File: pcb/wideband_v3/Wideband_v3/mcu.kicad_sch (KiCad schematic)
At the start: 42 parts, among them J1 Conn_01x10, J2 USB_C_Receptacle_USB2.0, J3 Tag connect, SW1 Key0, SW3 Key1, U1 RP2040, U2 W25Q128JVS, U8 AMS1117-3.3, Y1 12MHz

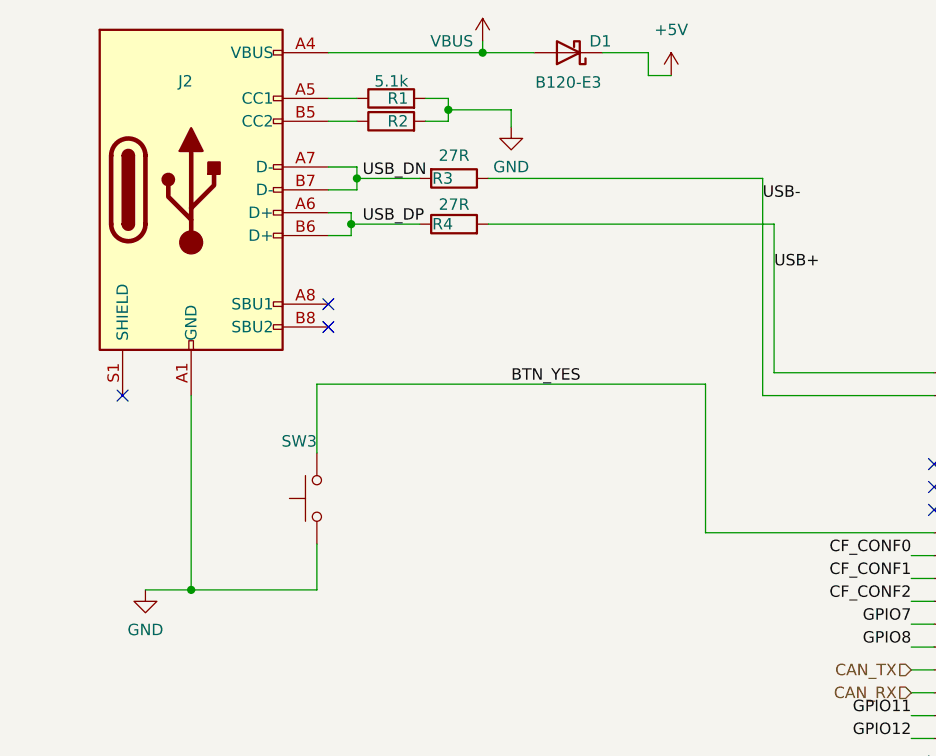
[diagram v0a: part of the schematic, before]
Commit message: rev3, reduce extended component count
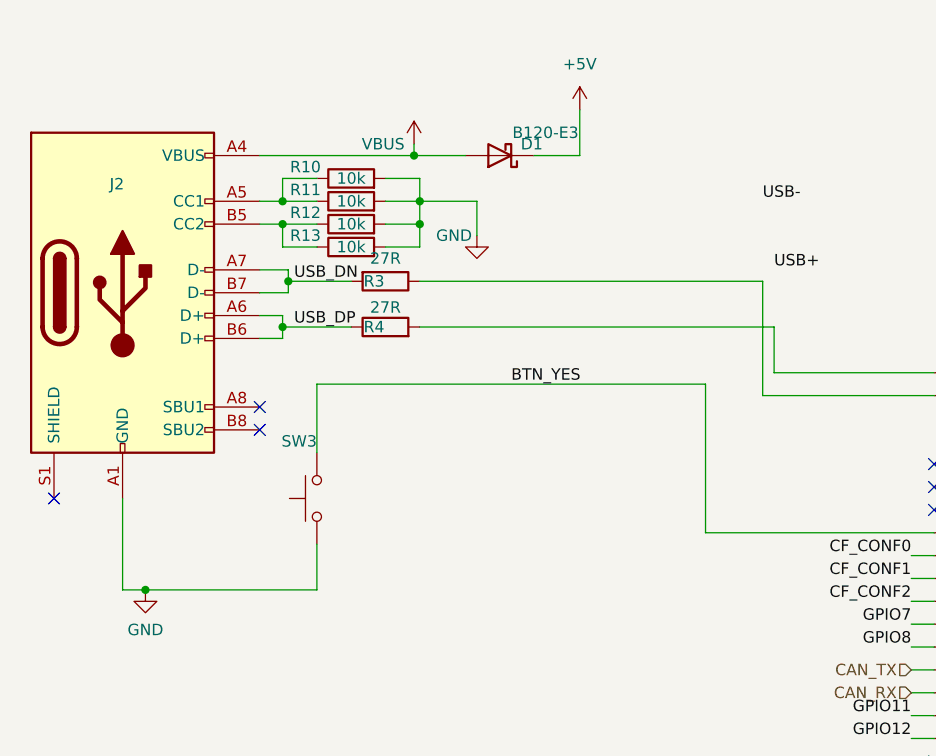
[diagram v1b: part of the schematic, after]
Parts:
- removed R1, R2: 5.1k, Resistor_SMD:R_0603_1608Metric, symbol Device:R
- added R10, R11, R12, R13: 10k, Resistor_SMD:R_0603_1608Metric, symbol Device:R
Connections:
- net GND: now also R10.2, R11.2, R12.2, R13.2
- net USB+: no longer R4.2, U1.47 (USB_DP)
- net USB-: no longer R3.1, U1.46 (USB_DM)
- net at J2.A5 (CC1): now also R10.1, R11.1
- net at J2.B5 (CC2): now also R12.1, R13.1
- new net: R3.1, U1.46 (USB_DM)
- new net: R4.2, U1.47 (USB_DP)
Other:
- moved on the sheet: D1, J2, R3, R4

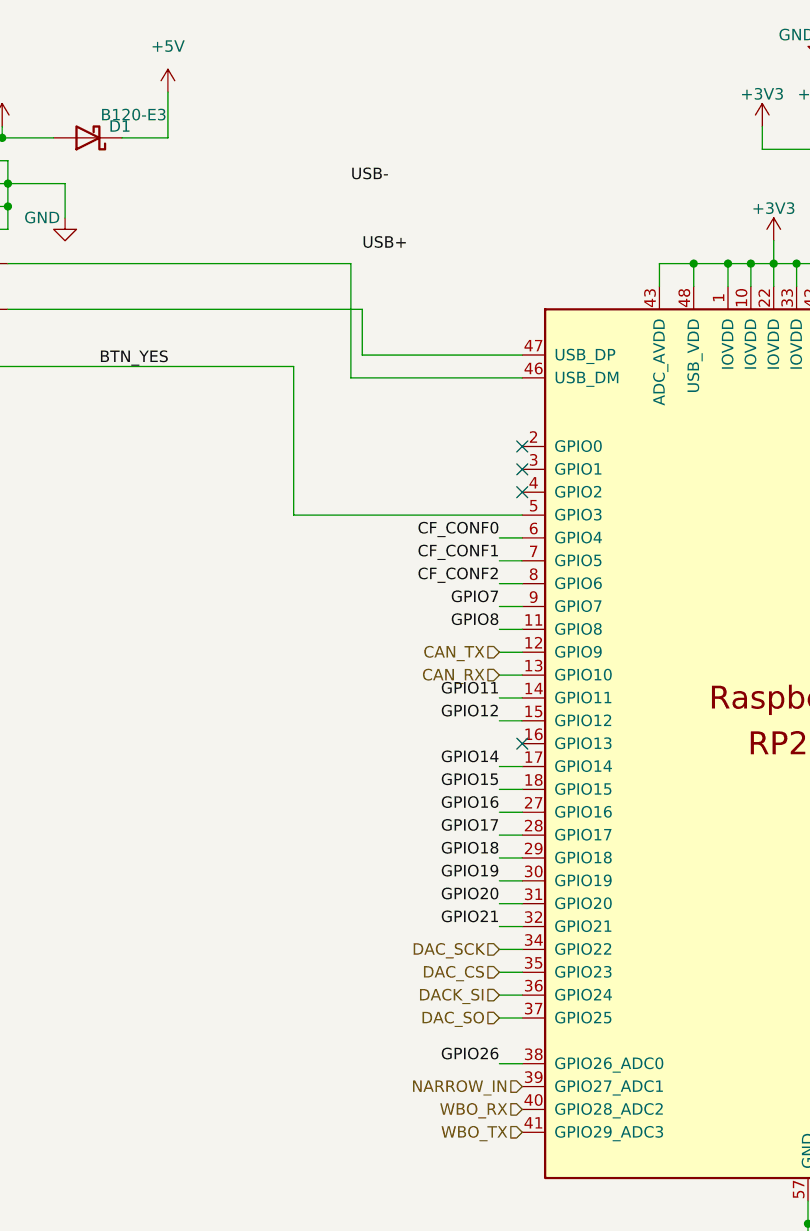
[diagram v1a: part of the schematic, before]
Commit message: Optimize SKUs
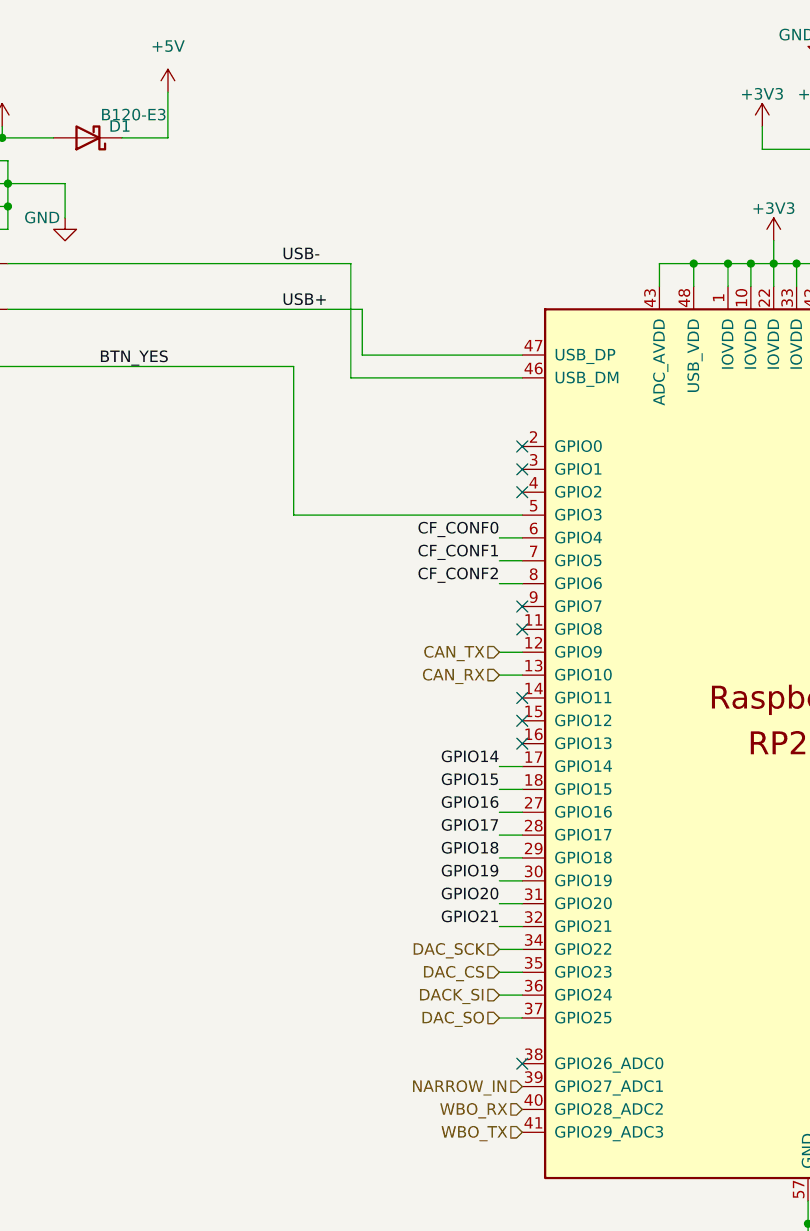
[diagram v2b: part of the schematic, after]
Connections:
- net USB+: now also R4.2, U1.47 (USB_DP)
- net USB-: now also R3.1, U1.46 (USB_DM)
- net GPIO11: no longer names the net of U1.14 (GPIO11)
- net GPIO12: no longer names the net of U1.15 (GPIO12)
- net GPIO26: no longer names the net of U1.38 (GPIO26_ADC0)
- net GPIO7: no longer names the net of U1.9 (GPIO7)
- net GPIO8: no longer names the net of U1.11 (GPIO8)
- no-connect marks 7 -> 12
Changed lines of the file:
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@@
+	)
+	(no_connect
+		(at 119.38 88.9)
+	)
+	(no_connect
+		(at 119.38 91.44)
+	)
+	(no_connect
+		(at 119.38 129.54)
+	)
+	(no_connect
+		(at 119.38 78.74)
 	)
 	(no_connect
@@
 	)
 	(no_connect
+		(at 119.38 81.28)
+	)
+	(no_connect
 		(at 44.45 57.15)
 	)
@@
 	(wire
 		(pts
-			(xy 116.84 91.44) (xy 119.38 91.44)
-		)
-		(stroke
-			(width 0)
-			(type default)
-		)
-	)
-	(wire
-		(pts
 			(xy 257.81 17.78) (xy 257.81 15.24)
 		)
@@
 	(wire
 		(pts
-			(xy 116.84 81.28) (xy 119.38 81.28)
-		)
-		(stroke
-			(width 0)
-			(type default)
-		)
-	)
-	(wire
-		(pts
 			(xy 248.92 17.78) (xy 248.92 15.24)
 		)
@@
 	(wire
 		(pts
-			(xy 116.84 78.74) (xy 119.38 78.74)
-		)
-		(stroke
-			(width 0)
-			(type default)
-		)
-	)
-	(wire
-		(pts
 			(xy 157.48 15.24) (xy 157.48 17.78)
 		)
@@
 	(wire
 		(pts
-			(xy 116.84 129.54) (xy 119.38 129.54)
-		)
-		(stroke
-			(width 0)
-			(type default)
-		)
-	)
-	(wire
-		(pts
 			(xy 24.13 165.1) (xy 36.83 165.1)
 		)
@@
 		(pts
 			(xy 264.16 152.4) (xy 269.24 152.4)
-		)
-		(stroke
-			(width 0)
-			(type default)
-		)
-	)
-	(wire
-		(pts
-			(xy 116.84 88.9) (xy 119.38 88.9)
 		)
 		(stroke
@@
 		)
 	)
-	(label "GPIO12"
-		(at 116.84 91.44 180)
-		(fields_autoplaced yes)
-		(effects
-			(font
-				(size 1.27 1.27)
-			)
-			(justify right bottom)
-		)
-	)
 	(label "NRST"
 		(at 185.42 113.03 0)
@@
 		)
 	)
-	(label "GPIO11"
-		(at 116.84 88.9 180)
-		(fields_autoplaced yes)
-		(effects
-			(font
-				(size 1.27 1.27)
-			)
-			(justify right bottom)
-		)
-	)
 	(label "GPIO19"
 		(at 26.67 180.34 0)
@@
 		)
 	)
-	(label "GPIO8"
-		(at 116.84 81.28 180)
-		(fields_autoplaced yes)
-		(effects
-			(font
-				(size 1.27 1.27)
-			)
-			(justify right bottom)
-		)
-	)
 	(label "USB+"
-		(at 101.6 39.37 0)
+		(at 92.71 45.72 0)
 		(fields_autoplaced yes)
 		(effects
@@
 			)
 			(justify left bottom)
-		)
-	)
-	(label "GPIO26"
-		(at 116.84 129.54 180)
-		(fields_autoplaced yes)
-		(effects
-			(font
-				(size 1.27 1.27)
-			)
-			(justify right bottom)
 		)
 	)
@@
 		)
 	)
-	(label "GPIO7"
-		(at 116.84 78.74 180)
-		(fields_autoplaced yes)
-		(effects
-			(font
-				(size 1.27 1.27)
-			)
-			(justify right bottom)
-		)
-	)
 	(label "GPIO19"
 		(at 116.84 109.22 180)
@@
 	)
 	(label "USB-"
-		(at 100.33 31.75 0)
-		(fields_autoplaced yes)
-		(effects
+		(at 92.71 40.64 0)
+		(fields_autoplaced yes)
+		(effects

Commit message: update DAC for v3
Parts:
- H1, H2, H3, H4, J1, J3, JP4, SW1: now left out of the parts list
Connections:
- net DACK_SI renamed DACK_SDA_2
- net DAC_CS renamed DAC_CLK_1
- net DAC_SCK renamed DAC_SDA_1
- net DAC_SO renamed DAC_CLK_2
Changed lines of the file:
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@@
 		)
 	)
-	(hierarchical_label "DAC_SCK"
+	(hierarchical_label "DAC_SDA_1"
 		(shape input)
 		(at 116.84 116.84 180)
@@
 		)
 	)
-	(hierarchical_label "DAC_SO"
+	(hierarchical_label "DAC_CLK_2"
 		(shape input)
 		(at 116.84 124.46 180)
@@
 		)
 	)
-	(hierarchical_label "DAC_CS"
+	(hierarchical_label "DAC_CLK_1"
 		(shape input)
 		(at 116.84 119.38 180)
@@
 		)
 	)
-	(hierarchical_label "DACK_SI"
+	(hierarchical_label "DACK_SDA_2"
 		(shape input)
 		(at 116.84 121.92 180)
@@
 		(unit 1)
 		(exclude_from_sim no)
-		(in_bom yes)
+		(in_bom no)
 		(on_board yes)
 		(dnp no)
@@
 		(unit 1)
 		(exclude_from_sim no)
-		(in_bom yes)
+		(in_bom no)
 		(on_board yes)
 		(dnp no)
@@
 		(unit 1)
 		(exclude_from_sim no)
-		(in_bom yes)
+		(in_bom no)
 		(on_board yes)
 		(dnp no)
@@
 		(unit 1)
 		(exclude_from_sim no)
-		(in_bom yes)
+		(in_bom no)
 		(on_board yes)
 		(dnp no)
@@
 		(unit 1)
 		(exclude_from_sim no)
-		(in_bom yes)
+		(in_bom no)
 		(on_board yes)
 		(dnp no)
@@
 		(unit 1)
 		(exclude_from_sim no)
-		(in_bom yes)
+		(in_bom no)
 		(on_board yes)
 		(dnp no)
@@
 		(unit 1)
 		(exclude_from_sim no)
-		(in_bom yes)
+		(in_bom no)
 		(on_board yes)
 		(dnp no)
@@
 		(unit 1)
 		(exclude_from_sim no)
-		(in_bom yes)
+		(in_bom no)
 		(on_board yes)
 		(dnp no)

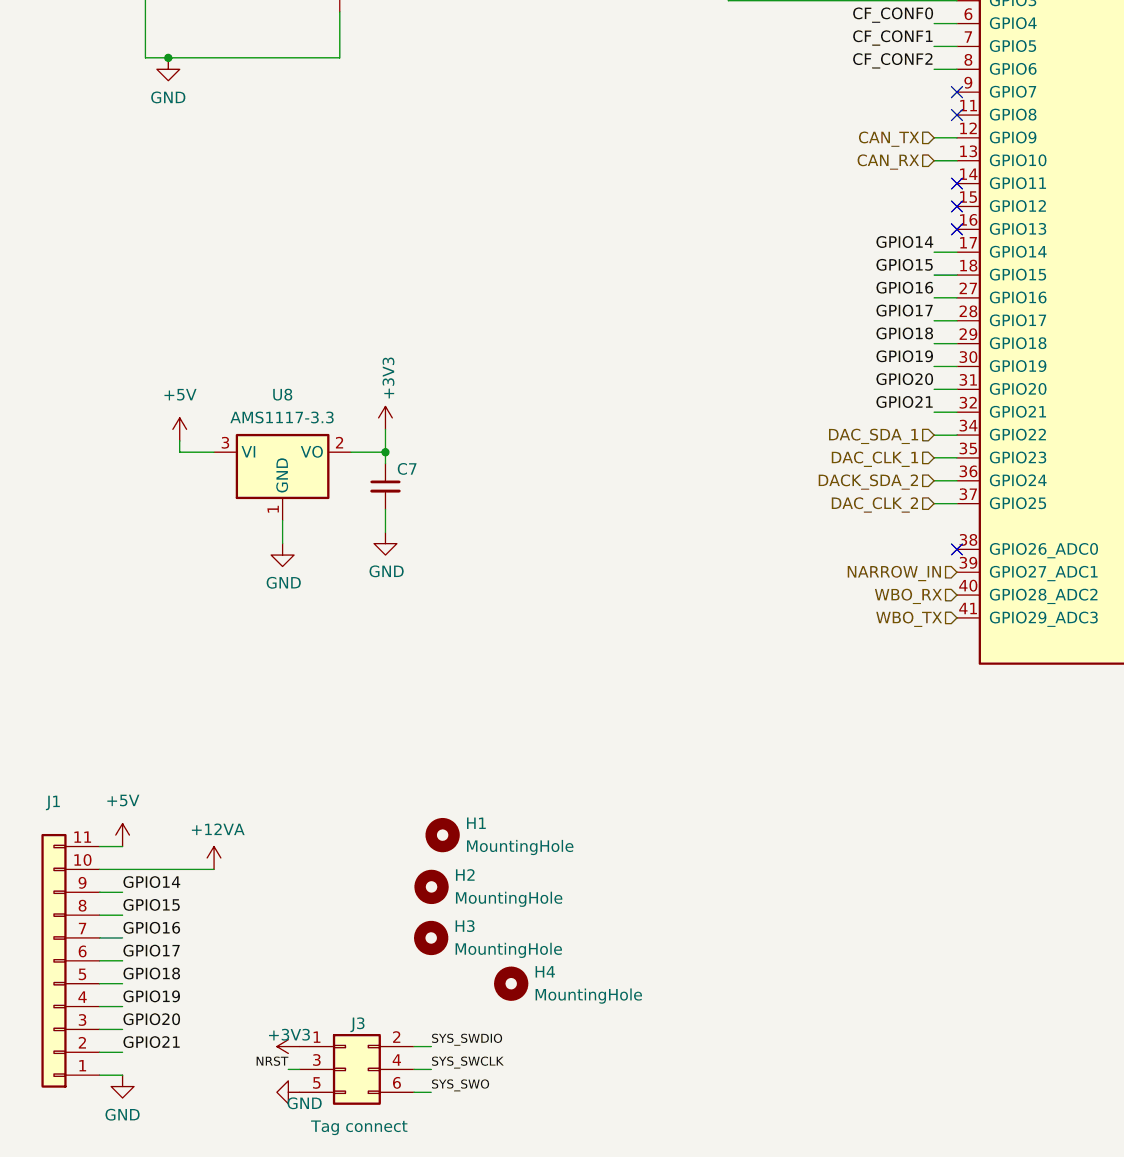
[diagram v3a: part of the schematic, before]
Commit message: rev3: update connector on main board
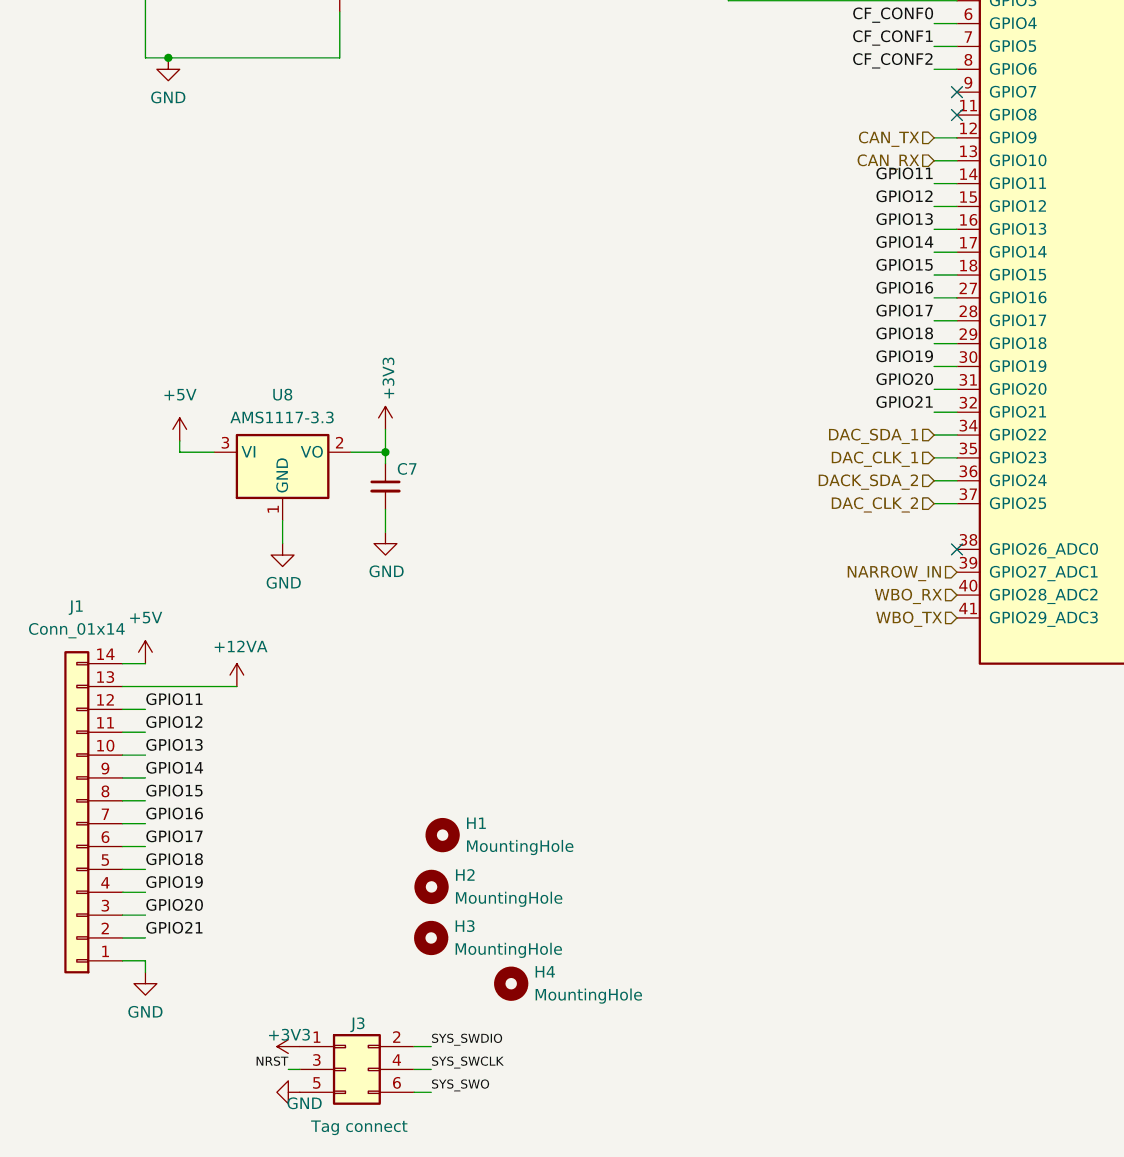
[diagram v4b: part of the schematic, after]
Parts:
- removed J1: Conn_01x10, Connector_PinHeader_2.00mm:PinHeader_1x11_P2.00mm_Vertical, symbol Connector_Generic:Conn_01x11
- added J1: Conn_01x14, Connector_PinHeader_2.54mm:PinHeader_2x07_P2.54mm_Vertical, symbol Connector_Generic:Conn_01x14
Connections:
- net +12VA: now also J1.13 (Pin_13)
- net +5V: now also J1.14 (Pin_14)
- net GND: now also J1.1 (Pin_1)
- net GPIO14: now also J1.9 (Pin_9)
- net GPIO15: now also J1.8 (Pin_8)
- net GPIO16: now also J1.7 (Pin_7)
- net GPIO17: now also J1.6 (Pin_6)
- net GPIO18: now also J1.5 (Pin_5)
- net GPIO19: now also J1.4 (Pin_4)
- net GPIO20: now also J1.3 (Pin_3)
- net GPIO21: now also J1.2 (Pin_2)
- net GPIO11: now reaches U1.14 (GPIO11)
- net GPIO11: now also J1.12 (Pin_12)
- net GPIO12: now reaches U1.15 (GPIO12)
- net GPIO12: now also J1.11 (Pin_11)
- net GPIO13: now reaches U1.16 (GPIO13)
- net GPIO13: now also J1.10 (Pin_10)
- no-connect marks 12 -> 9
